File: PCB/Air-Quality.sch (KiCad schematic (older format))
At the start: 18 parts, among them J2 Conn_01x04_Female, J3 Conn_01x07_Female, SW1 SW_Push, SW2 SW_SPST, U1 ARDUINO_MKR_ZERO

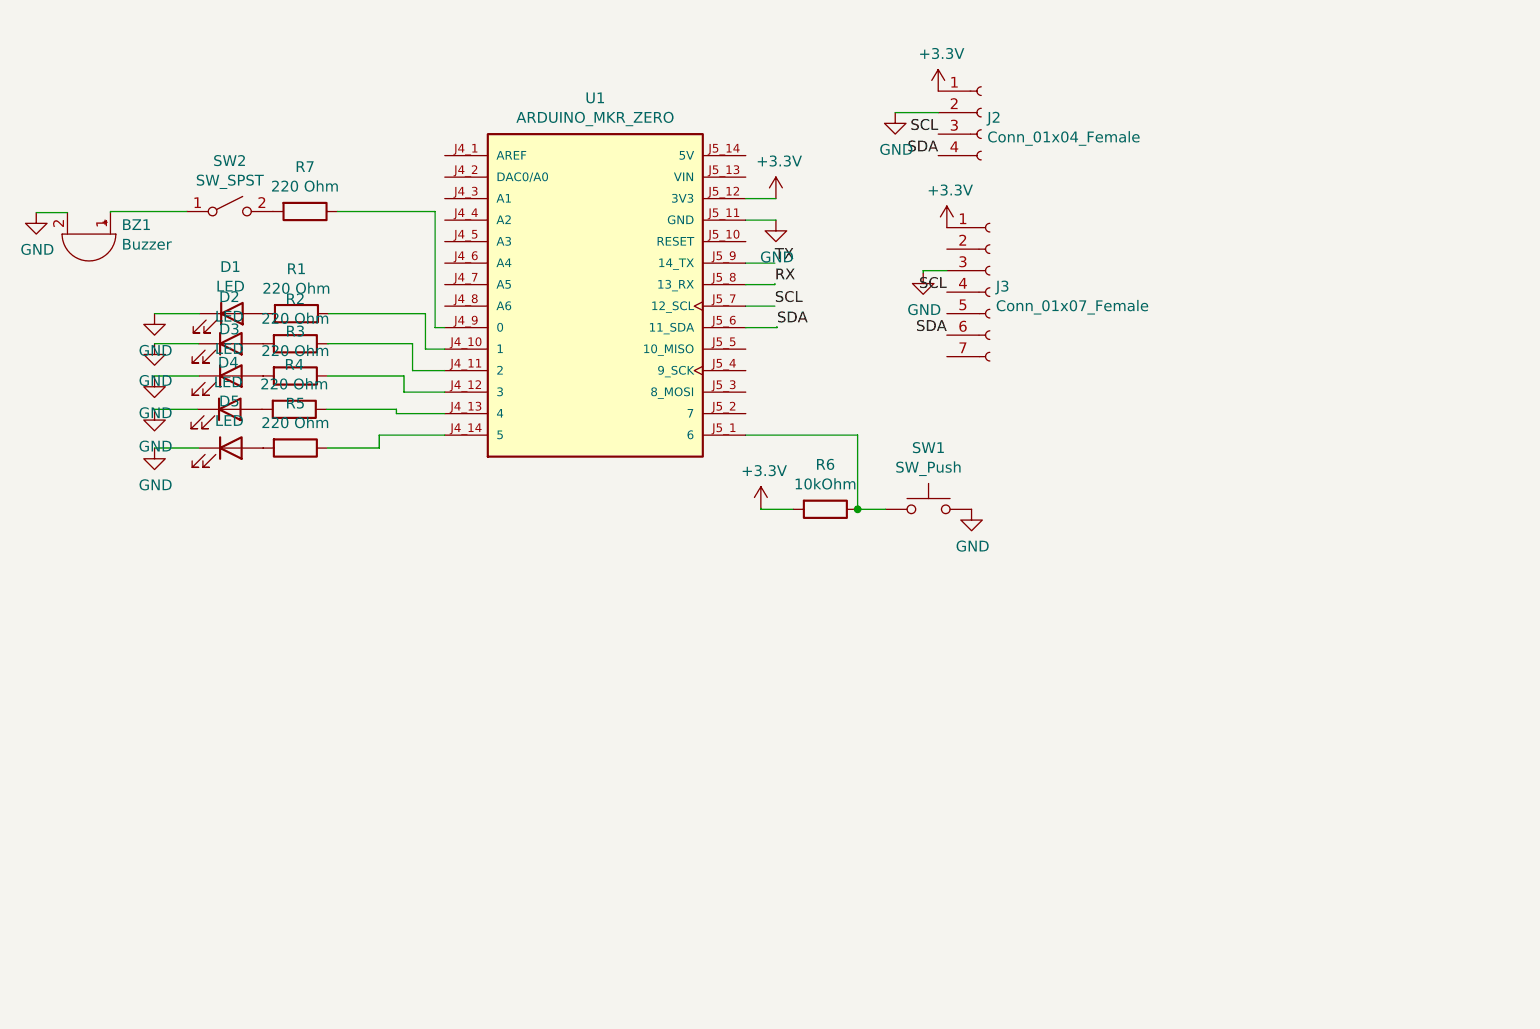
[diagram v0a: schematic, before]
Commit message: changed to RP 2040.
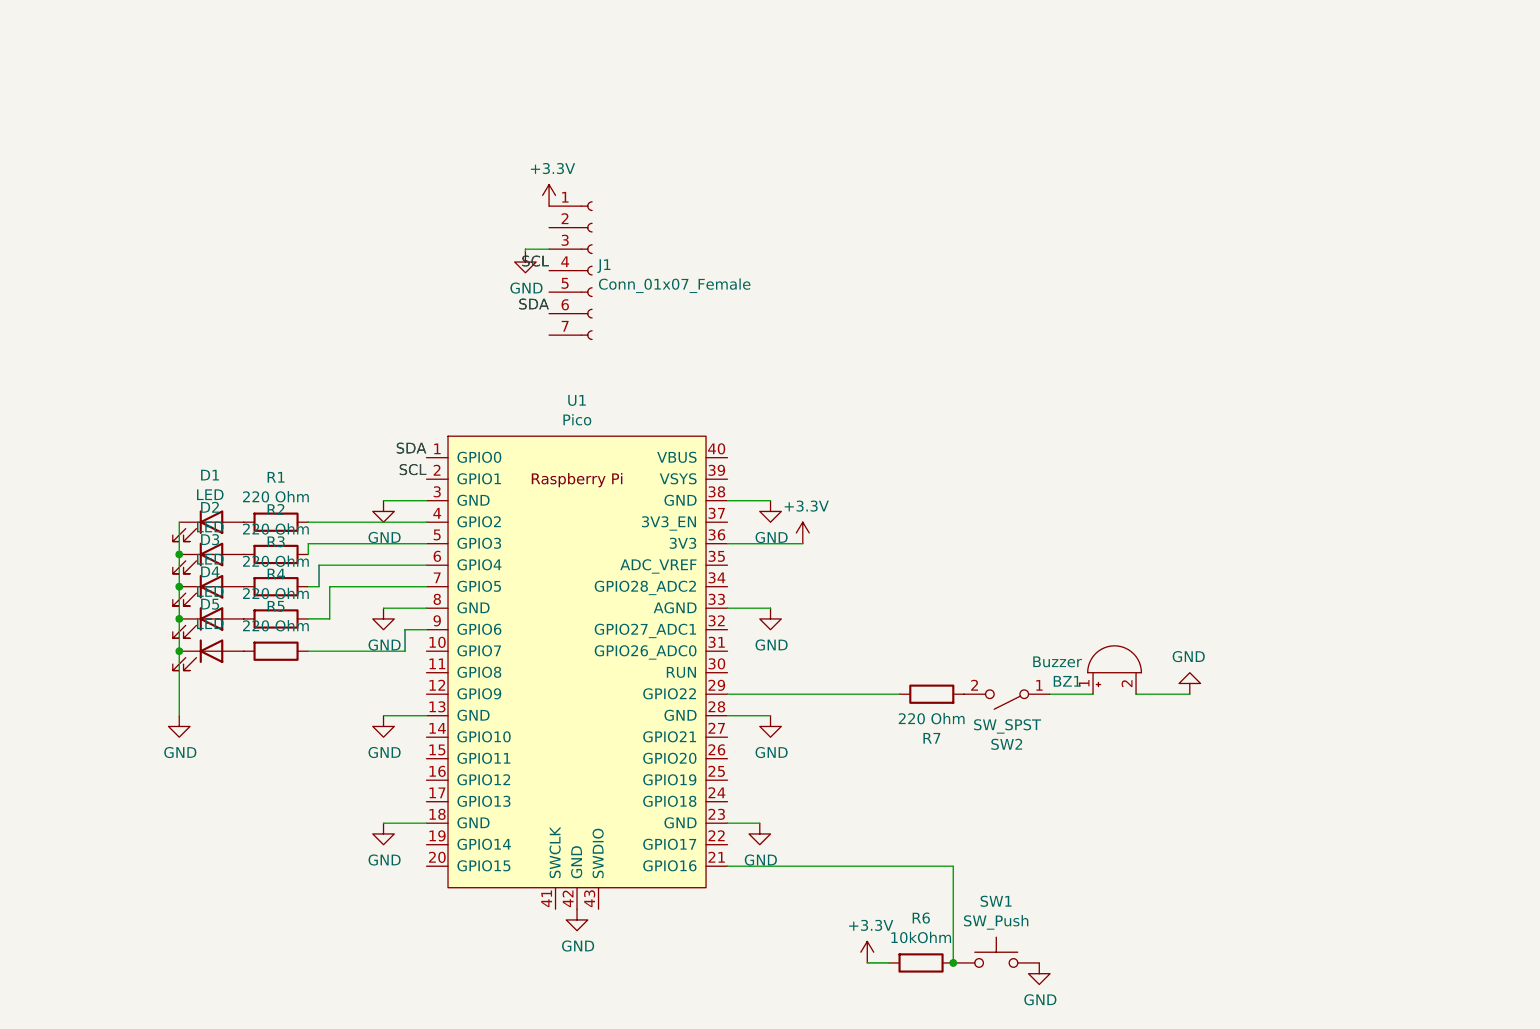
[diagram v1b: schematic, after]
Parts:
- removed J2: Conn_01x04_Female, Connector_PinHeader_2.54mm:PinHeader_1x04_P2.54mm_Vertical, symbol Connector:Conn_01x04_Female
- removed J3: Conn_01x07_Female, Connector_PinHeader_2.54mm:PinHeader_1x07_P2.54mm_Vertical, symbol Connector:Conn_01x07_Female
- removed U1: ARDUINO_MKR_ZERO, Arduino-MKR:MODULE_ARDUINO_MKR_ZERO, symbol Arduino-MKR:ARDUINO_MKR_ZERO
- added J1: Conn_01x07_Female, Connector_PinSocket_2.54mm:PinSocket_1x07_P2.54mm_Vertical, symbol Connector:Conn_01x07_Female
- added U1: Pico, MCU_RaspberryPI_and_Board:RPi_Pico_SMD_TH, symbol RaspberryPi_and_Board:Pico
- D1, D2, D3, D4, D5: footprint LED_THT:LED_D5.0mm_Clear -> LED_SMD:LED_0805_2012Metric
- R1, R2, R3, R4, R5, R6, R7: footprint Resistor_SMD:R_0805_2012Metric_Pad1.15x1.40mm_HandSolder -> Resistor_SMD:R_0805_2012Metric
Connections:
- net +3V3: now also J1.1 (Pin_1), U1.36 (3V3)
- net GND: now also J1.3 (Pin_3), U1.13 (GND), U1.18 (GND), U1.23 (GND), U1.28 (GND), U1.3 (GND), U1.33 (AGND), U1.38 (GND), U1.42 (GND), U1.8 (GND)
- net SCL: now also J1.4 (Pin_4), U1.2 (GPIO1)
- net SDA: now also J1.6 (Pin_6), U1.1 (GPIO0)
- net at R1.1: now also U1.4 (GPIO2)
- net at R2.1: now also U1.5 (GPIO3)
- net at R3.1: now also U1.6 (GPIO4)
- net at R4.1: now also U1.7 (GPIO5)
- net at R5.1: now also U1.9 (GPIO6)
- net at R7.1: now also U1.29 (GPIO22)
- net at R6.1, SW1.1: now also U1.21 (GPIO16)

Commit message: Small Buzzer. Wrong Sensor Configuration :-(
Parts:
- BZ1: footprint Buzzer_Beeper:Buzzer_12x9.5RM7.6 -> Buzzer_Beeper:PUIAudio_SMT_0825_S_4_R
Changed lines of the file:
@@
 F 0 "BZ1" V 6808 5352 50  0000 L CNN
 F 1 "Buzzer" V 6899 5352 50  0000 L CNN
-F 2 "Buzzer_Beeper:Buzzer_12x9.5RM7.6" V 6825 5300 50  0001 C CNN
+F 2 "Buzzer_Beeper:PUIAudio_SMT_0825_S_4_R" V 6825 5300 50  0001 C CNN
 F 3 "~" V 6825 5300 50  0001 C CNN
 	1    6850 5200

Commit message: Version 3 for friends.
Seeeduino
New Sensor
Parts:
- removed D1, D2, D3, D4, D5: LED, LED_SMD:LED_0805_2012Metric, symbol Device:LED
- removed R1, R2, R3, R4, R5: 220 Ohm, Resistor_SMD:R_0805_2012Metric, symbol Device:R
- removed R6: 10kOhm, Resistor_SMD:R_0805_2012Metric, symbol Device:R
- removed SW1: SW_Push, Button_Switch_THT:SW_PUSH_6mm, symbol Switch:SW_Push
- removed U1: Pico, MCU_RaspberryPI_and_Board:RPi_Pico_SMD_TH, symbol RaspberryPi_and_Board:Pico
- added H1, H2, H3, H4: MountingHole, MountingHole:MountingHole_2.7mm_M2.5_ISO14580, symbol Mechanical:MountingHole
- added U1: SeeeduinoXIAO, Seeeduino XIAO KICAD:Seeeduino XIAO-MOUDLE14P-2.54-21X17.8MM, symbol Seeeduino_XIAO:SeeeduinoXIAO
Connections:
- net +3V3: now also J1.3 (Pin_3), U1.12 (3V3); no longer J1.1 (Pin_1)
- net GND: now also J1.1 (Pin_1), U1.13 (GND), U1.16 (GND), U1.20 (GND); no longer J1.3 (Pin_3)
- net SCL: now also U1.6 (PA9_A5_D5_SCL)
- net SDA: now also J1.5 (Pin_5), U1.5 (PA8_A4_D4_SDA); no longer J1.6 (Pin_6)
- net at R7.1: now also U1.1 (PA02_A0_D0)
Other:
- moved on the sheet: BZ1, J1, R7, SW2
